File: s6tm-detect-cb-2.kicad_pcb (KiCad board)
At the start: 4 copper layers, 175 parts, among them J1 Conn_Coaxial, J2 Conn_01x04_Pin, J3 USB_C_Receptacle_USB2.0_14P, J4 Conn_01x04, J5 Conn_01x04, J6 USB_C_Receptacle_USB2.0_14P, J7 Conn_01x04_Pin, J8 SIM_Card_Shielded, J9 Conn_Coaxial, Q1 AO3400A, Q2 MMBT3904, Q3 MMBT3904, Q4 MMBT3904, SW1 SW_Push, SW2 SW_Push, SW3 SW_Push, SW4 SW_Push, U1 W25Q128JVS, U10 TPS6282x, U11 TPS6282x, U12 TPS259472A, U13 TPD3F303DPV, U14 SIM7080G, U15 SN74LV1T125DBV, U16 SN74LV1T125DBV, U17 SN74LV1T125DBV, U18 SN74LV1T125DBV, U19 SN74LV1T125DBV, U2 SN65HVD230, U3 PCF85263ATL, U4 MS5607, U5 ESP32-S3FH4R2, U6 HTU21, U8 VL53L0CXV0DH1, U9 NextPM, Y1 32k768, Y2 48M

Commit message: schem: update gnd net class priority
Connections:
- C40 pad 2: Net-(J8-VCC) -> unconnected-(C40-Pad2)
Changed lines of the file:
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@@
 		(sheetname "/")
 		(sheetfile "s6tm-detect-cb-2.kicad_sch")
+		(units
+			(unit
+				(name "A")
+				(pins "1" "2")
+			)
+		)
 		(attr smd)
 		(duplicate_pad_numbers_are_jumpers no)
@@
 			(layers "F.Cu" "F.Mask" "F.Paste")
 			(roundrect_rratio 0.25)
-			(net "Net-(Q3-PadB)")
+			(net "Net-(Q3-B)")
 			(pintype "passive")
 		)
@@
 			(layers "F.Cu" "F.Mask" "F.Paste")
 			(roundrect_rratio 0.25)
-			(net "Net-(Q2-PadB)")
+			(net "Net-(Q2-B)")
 			(pintype "passive")
 		)
@@
 			(layers "F.Cu" "F.Mask" "F.Paste")
 			(roundrect_rratio 0.25)
-			(net "Net-(Q4-PadE)")
+			(net "Net-(Q4-B)")
 			(pinfunction "B_1")
 			(pintype "input")
@@
 			(layers "F.Cu" "F.Mask" "F.Paste")
 			(roundrect_rratio 0.25)
-			(net "Net-(U14-~{PWRKEY})")
+			(net "Net-(Q4-C)")
 			(pinfunction "C_3")
 			(pintype "passive")
@@
 			(layers "F.Cu" "F.Mask" "F.Paste")
 			(roundrect_rratio 0.25)
-			(net "Net-(Q2-PadB)")
+			(net "Net-(Q2-B)")
 			(pinfunction "B_1")
 			(pintype "input")
@@
 			(layers "F.Cu" "F.Mask" "F.Paste")
 			(roundrect_rratio 0.25)
-			(net "Net-(U14-~{PWRKEY})")
+			(net "Net-(Q4-C)")
 			(pintype "passive")
 		)
@@
 			(layers "F.Cu" "F.Mask" "F.Paste")
 			(roundrect_rratio 0.25)
-			(net "Net-(Q3-PadB)")
+			(net "Net-(Q3-B)")
 			(pinfunction "B_1")
 			(pintype "input")
@@
 			(size 2 2)
 			(layers "F.Cu" "F.Mask")
-			(net "Net-(U14-~{PWRKEY})")
+			(net "Net-(Q4-C)")
 			(pinfunction "1_1")
 			(pintype "passive")
@@
 			(size 0.6 1.6)
 			(layers "F.Cu" "F.Mask")
-			(net "Net-(U14-~{PWRKEY})")
+			(net "Net-(Q4-C)")
 			(pinfunction "~{PWRKEY}_39")
 			(pintype "input")
@@
 			(layers "F.Cu" "F.Mask" "F.Paste")
 			(roundrect_rratio 0.25)
-			(net "Net-(J8-VCC)")
+			(net "unconnected-(C40-Pad2)")
 			(pintype "passive")
 		)
@@
 			(layers "F.Cu" "F.Mask" "F.Paste")
 			(roundrect_rratio 0.25)
-			(net "Net-(Q4-PadE)")
+			(net "Net-(Q4-B)")
 			(pintype "passive")
 		)
@@
 			(layers "F.Cu" "F.Mask" "F.Paste")
 			(roundrect_rratio 0.25)
-			(net "Net-(Q4-PadE)")
+			(net "Net-(Q4-B)")
 			(pintype "passive")
 		)
@@
 			(layers "F.Cu" "F.Mask" "F.Paste")
 			(roundrect_rratio 0.25)
-			(net "Net-(Q2-PadB)")
+			(net "Net-(Q2-B)")
 			(pintype "passive")
 		)
@@
 			(layers "F.Cu" "F.Mask" "F.Paste")
 			(roundrect_rratio 0.25)
-			(net "Net-(Q3-PadB)")
+			(net "Net-(Q3-B)")
 			(pintype "passive")
 		)

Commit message: pcb: initial sectionning
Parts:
- moved L5 191.3 mm to (274.3, 162.7)
- moved U11 189.4 mm to (278.4, 163.0)
- moved TP6 188.5 mm to (278.1, 158.1)
- moved R20 181.0 mm to (274.1, 159.9)
- moved C25 180.8 mm to (274.1, 157.3)
- moved L4 180.2 mm to (262.9, 155.8)
- moved C30 174.1 mm to (270.6, 161.0)
- moved C28 173.9 mm to (270.6, 159.0)
- moved C26 173.8 mm to (270.6, 157.1)
- moved TP7 173.2 mm to (262.6, 159.3)
- moved U10 173.2 mm to (262.4, 163.2)
- moved R18 171.9 mm to (273.5, 165.2)
- moved C34 170.8 mm to (270.6, 165.0)
- moved C32 170.7 mm to (270.6, 163.0)
- moved D8 168.6 mm to (245.3, 159.8), turned to 90 degrees
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
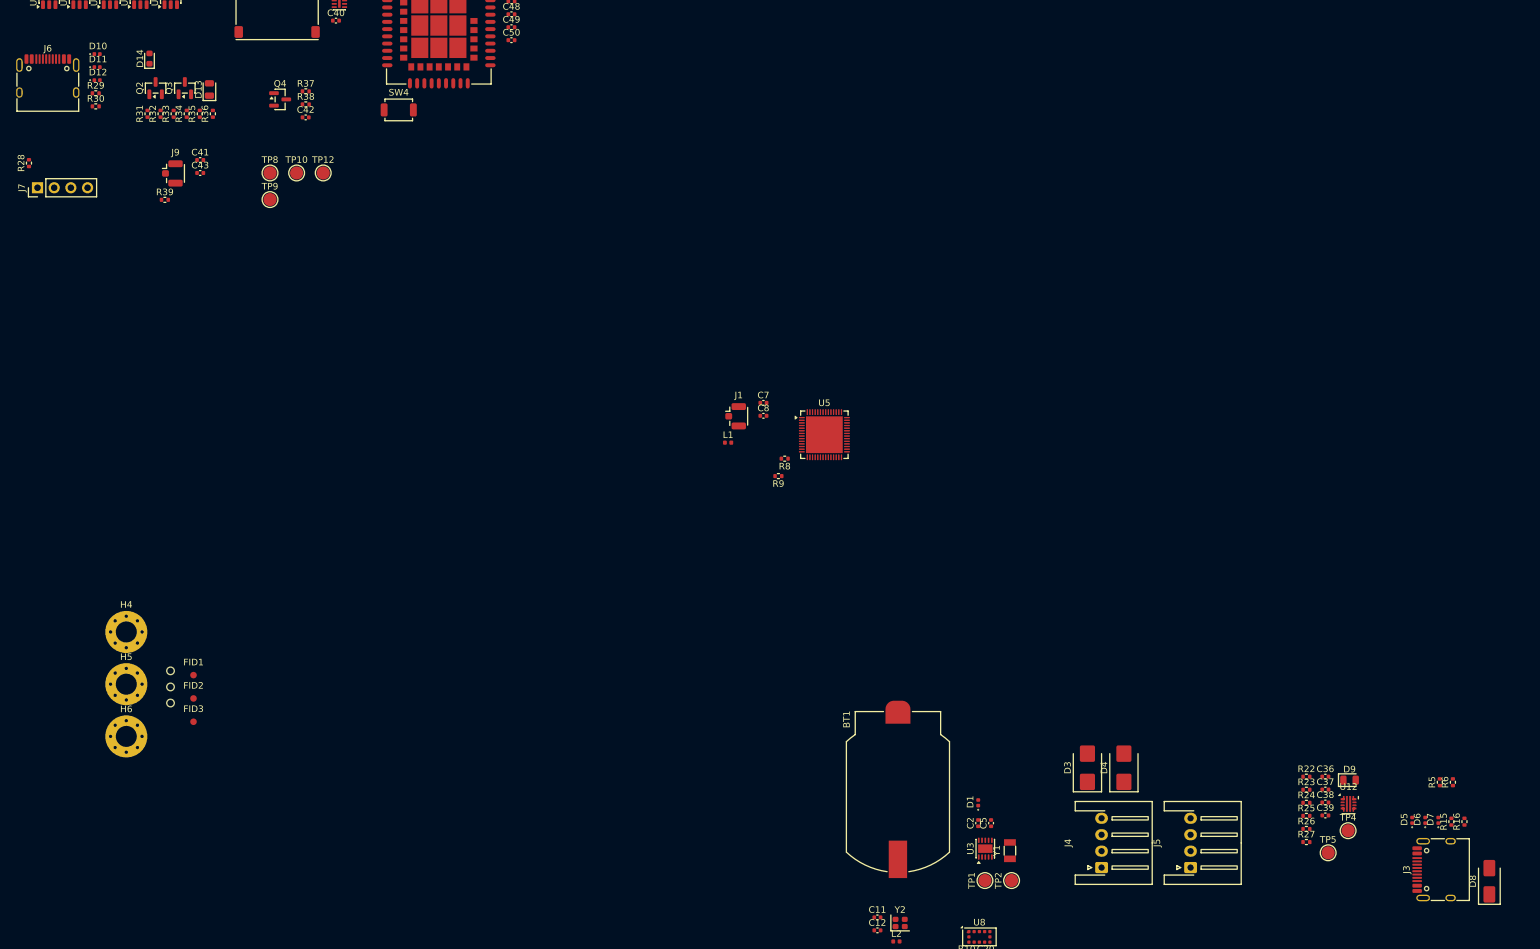
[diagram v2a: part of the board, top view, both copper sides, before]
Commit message: pcb: add usb c layout
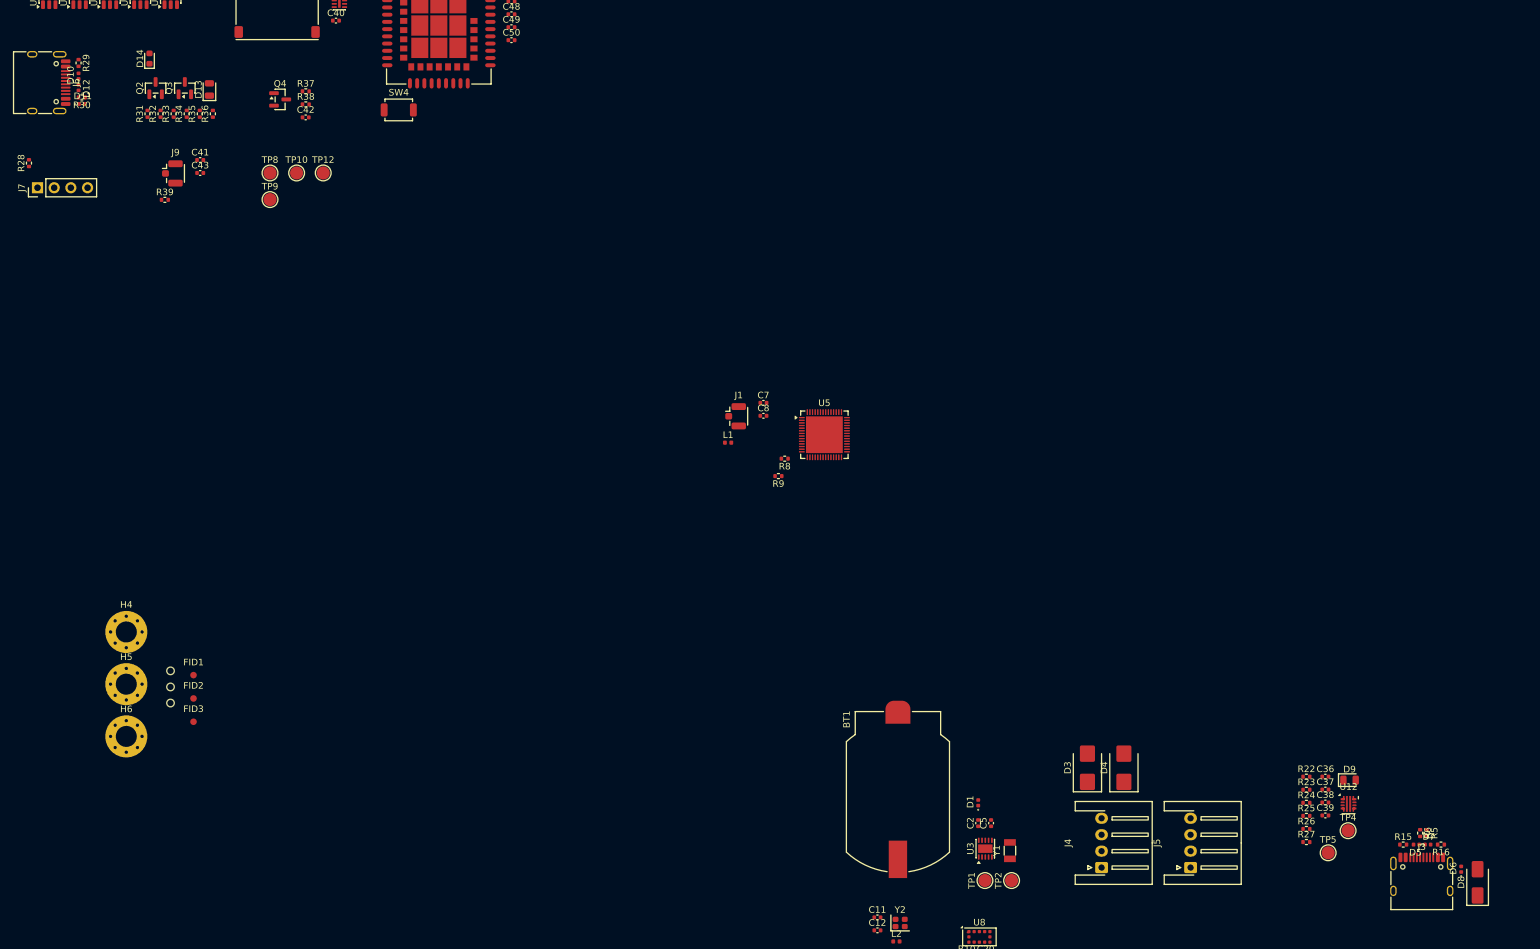
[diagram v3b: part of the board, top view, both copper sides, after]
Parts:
- moved D6 9.24 mm to (241.0, 158.0)
- moved R6 9.21 mm to (234.8, 152.5), turned to -90 degrees
- moved R15 8.12 mm to (232.2, 154.2), turned to 0 degrees
- moved R5 7.99 mm to (235.8, 152.5), turned to -90 degrees
- moved D11 6.07 mm to (31.0, 41.5)
- moved R29 5.31 mm to (30.5, 35.2), turned to -90 degrees
- moved R16 5.00 mm to (237.9, 154.2), turned to 180 degrees
- moved D10 4.38 mm to (30.5, 37.2), turned to 90 degrees
- moved D7 4.02 mm to (235.9, 154.2), turned to 0 degrees
- moved J3 3.99 mm to (235.0, 160.2), turned to 0 degrees
- moved D5 3.75 mm to (234.2, 154.2), turned to 180 degrees
- moved D12 3.04 mm to (30.5, 39.0), turned to -90 degrees
- moved R30 2.52 mm to (31.0, 40.5), turned to 180 degrees
- moved D8 1.80 mm to (243.5, 160.0)
- moved J6 1.39 mm to (24.5, 38.2), turned to -90 degrees

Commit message: pcb: add flash layout
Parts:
- moved C4 10.9 mm to (136.5, 172.2), turned to 0 degrees
- moved C3 9.66 mm to (135.0, 173.5), turned to -90 degrees
- moved R1 7.60 mm to (135.0, 181.5), turned to -90 degrees
- moved U1 1.07 mm to (138.0, 177.5)
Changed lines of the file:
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@@
 	(footprint "Package_SO:SOIC-8_5.3x5.3mm_P1.27mm"
 		(layer "F.Cu")
-		(at 137.155 176.8375 90)
+		(at 138 177.5 90)
 		(descr "SOIC, 8 Pin (JEITA/EIAJ ED-7311-19 variation 08-001-BBA and Atmel/Microchip, 208 mils width, https://www.jeita.or.jp/japanese/standard/book/ED-7311-19/#target/page_no=21, https://ww1.microchip.com/downloads/en/DeviceDoc/20005045C.pdf#page=23, https://ww1.microchip.com/downloads/en/DeviceDoc/doc2535.pdf#page=162)")
 		(tags "SOIC SO P-SOP SOP SOP-8 SO SO-8 8S2 S2AE/F K04-056 CASE-751BE SO8W 8-Pin-SOIC PSA W8-2 W8-4 W8MS-1 FPT-8P-M08")
@@
 	(footprint "Capacitor_SMD:C_0402_1005Metric"
 		(layer "F.Cu")
-		(at 143.53 180.5775 90)
+		(at 136.5 172.25)
 		(descr "Capacitor SMD 0402 (1005 Metric), square (rectangular) end terminal, IPC-7351 nominal, (Body size source: IPC-SM-782 page 76, https://www.pcb-3d.com/wordpress/wp-content/uploads/ipc-sm-782a_amendment_1_and_2.pdf)")
 		(tags "capacitor")
 		(property "Reference" "C4"
-			(at 0 -1.16 90)
+			(at 0 -1.16 0)
 			(layer "F.SilkS")
 			(effects
@@
 		)
 		(property "Value" "0u1"
-			(at 0 1.16 90)
+			(at 0 1.16 0)
 			(layer "F.Fab")
 			(effects
@@
 		)
 		(property "Datasheet" ""
-			(at 0 0 90)
+			(at 0 0 0)
 			(layer "F.Fab")
 			(hide yes)
@@
 		)
 		(property "Description" "Unpolarized capacitor"
-			(at 0 0 90)
+			(at 0 0 0)
 			(layer "F.Fab")
 			(hide yes)
@@
 		)
 		(property "KiLib_Generator" "SMD_2terminal_chip_molded"
-			(at 0 0 90)
+			(at 0 0 0)
 			(layer "F.SilkS")
 			(hide yes)
@@
 		)
 		(property "Manufacturer" "Samsung Electro-Mechanics "
-			(at 0 0 90)
+			(at 0 0 0)
 			(unlocked yes)
 			(layer "F.Fab")
@@
 		)
 		(property "Manufacturer Part Number" "CL05B104KB54PNC"
-			(at 0 0 90)
+			(at 0 0 0)
 			(unlocked yes)
 			(layer "F.Fab")
@@
 		)
 		(property "Basic" "Y"
-			(at 0 0 90)
+			(at 0 0 0)
 			(unlocked yes)
 			(layer "F.Fab")
@@
 		)
 		(property "JLCPCB Part #" "C307331"
-			(at 0 0 90)
+			(at 0 0 0)
 			(unlocked yes)
 			(layer "F.Fab")
@@
 		)
 		(property "KLC_S3.3" ""
-			(at 0 0 90)
+			(at 0 0 0)
 			(unlocked yes)
 			(layer "F.Fab")
@@
 		)
 		(property "KLC_S4.1" ""
-			(at 0 0 90)
+			(at 0 0 0)
 			(unlocked yes)
 			(layer "F.Fab")
@@
 		)
 		(fp_text user "${REFERENCE}"
-			(at 0 0 90)
+			(at 0 0 0)
 			(layer "F.Fab")
 			(effects
@@
 		)
 		(pad "1" smd roundrect
-			(at -0.48 0 90)
+			(at -0.48 0)
 			(size 0.56 0.62)
 			(layers "F.Cu" "F.Mask" "F.Paste")
@@
 		)
 		(pad "2" smd roundrect
-			(at 0.48 0 90)
+			(at 0.48 0)
 			(size 0.56 0.62)
 			(layers "F.Cu" "F.Mask" "F.Paste")
@@
 	(footprint "Capacitor_SMD:C_0402_1005Metric"
 		(layer "F.Cu")
-		(at 141.56 180.5775 90)
+		(at 135 173.48 -90)
 		(descr "Capacitor SMD 0402 (1005 Metric), square (rectangular) end terminal, IPC-7351 nominal, (Body size source: IPC-SM-782 page 76, https://www.pcb-3d.com/wordpress/wp-content/uploads/ipc-sm-782a_amendment_1_and_2.pdf)")
 		(tags "capacitor")
@@
 		)
 		(property "Manufacturer" "Samsung Electro-Mechanics "
-			(at 0 0 90)
+			(at 0 0 270)
 			(unlocked yes)
 			(layer "F.Fab")
@@
 		)
 		(property "Manufacturer Part Number" "CL05A105KA5NQNC"
-			(at 0 0 90)
+			(at 0 0 270)
 			(unlocked yes)
 			(layer "F.Fab")
@@
 		)
 		(property "Basic" "Y"
-			(at 0 0 90)
+			(at 0 0 270)
 			(unlocked yes)
 			(layer "F.Fab")
@@
 		)
 		(property "JLCPCB Part #" "C52923"
-			(at 0 0 90)
+			(at 0 0 270)
 			(unlocked yes)
 			(layer "F.Fab")
@@
 		)
 		(property "KLC_S3.3" ""
-			(at 0 0 90)
+			(at 0 0 270)
 			(unlocked yes)
 			(layer "F.Fab")
@@
 		)
 		(property "KLC_S4.1" ""
-			(at 0 0 90)
+			(at 0 0 270)
 			(unlocked yes)
 			(layer "F.Fab")
@@
 		(duplicate_pad_numbers_are_jumpers no)
 		(fp_line
-			(start -0.107836 -0.36)
-			(end 0.107836 -0.36)
+			(start -0.107836 0.36)
+			(end 0.107836 0.36)
 			(stroke
 				(width 0.12)
@@
 		)
 		(fp_line
-			(start -0.107836 0.36)
-			(end 0.107836 0.36)
+			(start -0.107836 -0.36)
+			(end 0.107836 -0.36)
 			(stroke
 				(width 0.12)
@@
 		)
 		(pad "1" smd roundrect
-			(at -0.48 0 90)
+			(at -0.48 0 270)
 			(size 0.56 0.62)
 			(layers "F.Cu" "F.Mask" "F.Paste")
@@
 		)
 		(pad "2" smd roundrect
-			(at 0.48 0 90)
+			(at 0.48 0 270)
 			(size 0.56 0.62)
 			(layers "F.Cu" "F.Mask" "F.Paste")
@@
 	(footprint "Resistor_SMD:R_0402_1005Metric"
 		(layer "F.Cu")
-		(at 141.57 177.6875 90)
+		(at 135 181.5 -90)
 		(descr "Resistor SMD 0402 (1005 Metric), square (rectangular) end terminal, IPC-7351 nominal, (Body size source: IPC-SM-782 page 72, https://www.pcb-3d.com/wordpress/wp-content/uploads/ipc-sm-782a_amendment_1_and_2.pdf)")
 		(tags "resistor")
@@
 		)
 		(property "Basic" "Y"
-			(at 0 0 90)
+			(at 0 0 270)
 			(unlocked yes)
 			(layer "F.Fab")
@@
 		)
 		(property "JLCPCB Part #" "C25744"
-			(at 0 0 90)
+			(at 0 0 270)
 			(unlocked yes)
 			(layer "F.Fab")
@@
 		)
 		(property "Manufacturer" "Uniroyal Elec"
-			(at 0 0 90)
+			(at 0 0 270)
 			(unlocked yes)
 			(layer "F.Fab")
@@
 		)
 		(property "Manufacturer Part Number" "0402WGF1002TCE"
-			(at 0 0 90)
+			(at 0 0 270)
 			(unlocked yes)
 			(layer "F.Fab")
@@
 		)
 		(property "KLC_S3.3" ""
-			(at 0 0 90)
+			(at 0 0 270)
 			(unlocked yes)
 			(layer "F.Fab")
@@
 		)
 		(property "KLC_S4.1" ""
-			(at 0 0 90)
+			(at 0 0 270)
 			(unlocked yes)
 			(layer "F.Fab")
@@
 		(duplicate_pad_numbers_are_jumpers no)
 		(fp_line
-			(start -0.153641 -0.38)
-			(end 0.153641 -0.38)
+			(start -0.153641 0.38)
+			(end 0.153641 0.38)
 			(stroke
 				(width 0.12)
@@
 		)
 		(fp_line
-			(start -0.153641 0.38)
-			(end 0.153641 0.38)
+			(start -0.153641 -0.38)
+			(end 0.153641 -0.38)
 			(stroke
 				(width 0.12)
@@
 		)
 		(pad "1" smd roundrect
-			(at -0.51 0 90)
+			(at -0.51 0 270)
 			(size 0.54 0.64)
 			(layers "F.Cu" "F.Mask" "F.Paste")
@@
 		)
 		(pad "2" smd roundrect
-			(at 0.51 0 90)
+			(at 0.51 0 270)
 			(size 0.54 0.64)
 			(layers "F.Cu" "F.Mask" "F.Paste")

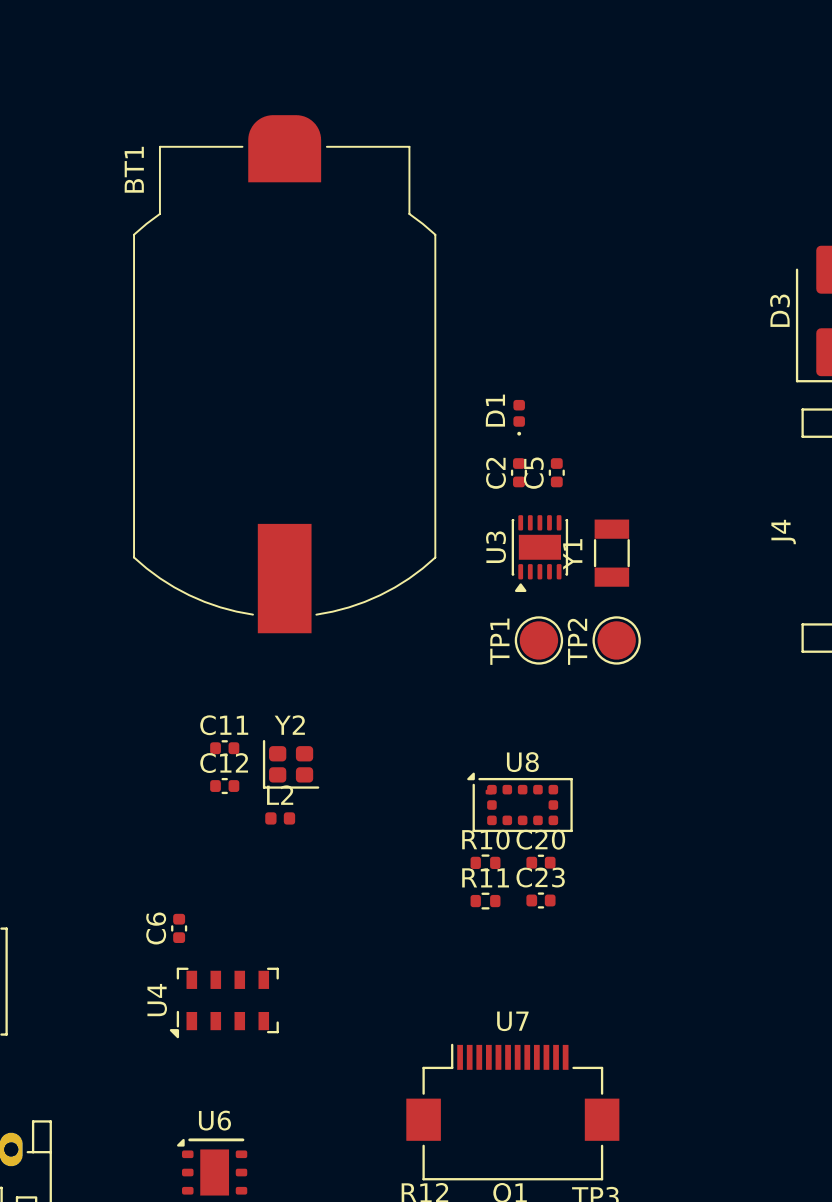
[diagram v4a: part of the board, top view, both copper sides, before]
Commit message: pcb: add rtc layout
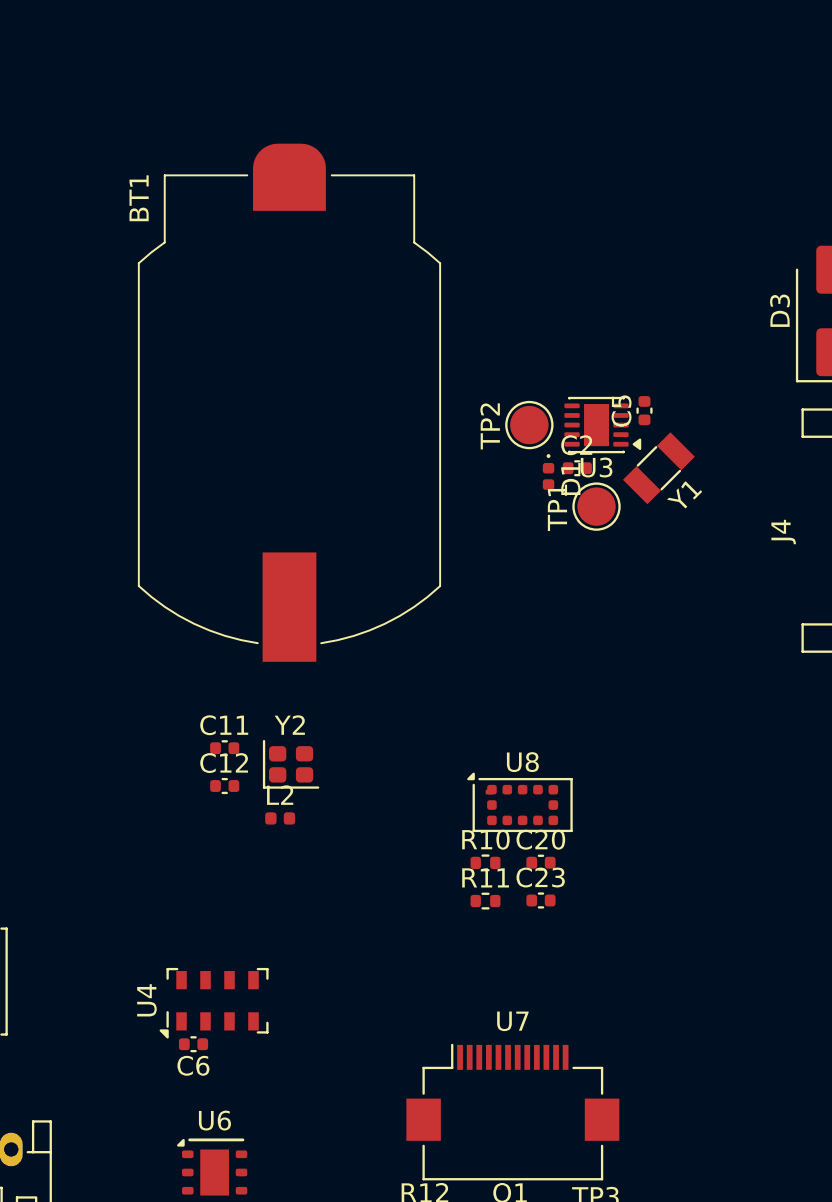
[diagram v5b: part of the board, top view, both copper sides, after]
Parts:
- moved TP2 12.1 mm to (168.0, 148.5)
- moved TP1 7.59 mm to (171.5, 152.8)
- moved U3 7.02 mm to (171.5, 148.5), turned to 180 degrees
- moved C6 6.08 mm to (150.5, 180.8), turned to 180 degrees
- moved C5 5.60 mm to (174.0, 147.8)
- moved Y1 5.06 mm to (174.8, 150.8), turned to -135 degrees
- moved D1 3.62 mm to (169.0, 151.2), turned to -90 degrees
- moved C2 3.05 mm to (170.5, 150.8), turned to 0 degrees
- moved BT1 1.51 mm to (155.5, 148.5)
- moved U4 0.54 mm to (151.8, 178.5)

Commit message: pcb: add esp32 layout
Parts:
- moved C17 123.8 mm to (145.0, 86.2)
- moved C14 122.8 mm to (148.5, 93.8)
- moved C18 120.7 mm to (140.8, 86.3)
- moved C10 120.4 mm to (135.0, 90.2)
- moved C13 119.9 mm to (136.0, 90.2)
- moved C15 119.5 mm to (138.5, 89.8), turned to 180 degrees
- moved L3 119.0 mm to (137.0, 90.2)
- moved C16 114.6 mm to (143.2, 97.3), turned to -90 degrees
- moved C12 83.9 mm to (144.8, 83.8), turned to -90 degrees
- moved L2 83.8 mm to (142.0, 86.2), turned to 90 degrees
- moved Y2 83.4 mm to (142.8, 83.8)
- moved C11 82.4 mm to (140.8, 83.8), turned to -90 degrees
- moved L1 11.1 mm to (138.5, 86.8), turned to -45 degrees
- moved J1 6.98 mm to (135.2, 83.5), turned to 135 degrees
- moved C8 4.58 mm to (139.2, 88.0), turned to -135 degrees
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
